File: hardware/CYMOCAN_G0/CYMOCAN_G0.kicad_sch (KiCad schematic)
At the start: 38 parts, among them J1 105450-0101, J2 CAN2 TX|RX, J3 Conn_01x02_Pin, J4 Conn_01x02_Pin, J5 CAN2, J6 DebugEdge_02x05, J7 CAN1 TX|RX, J8 CAN1, SW1 Reset, U1 AP2112K-3.3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

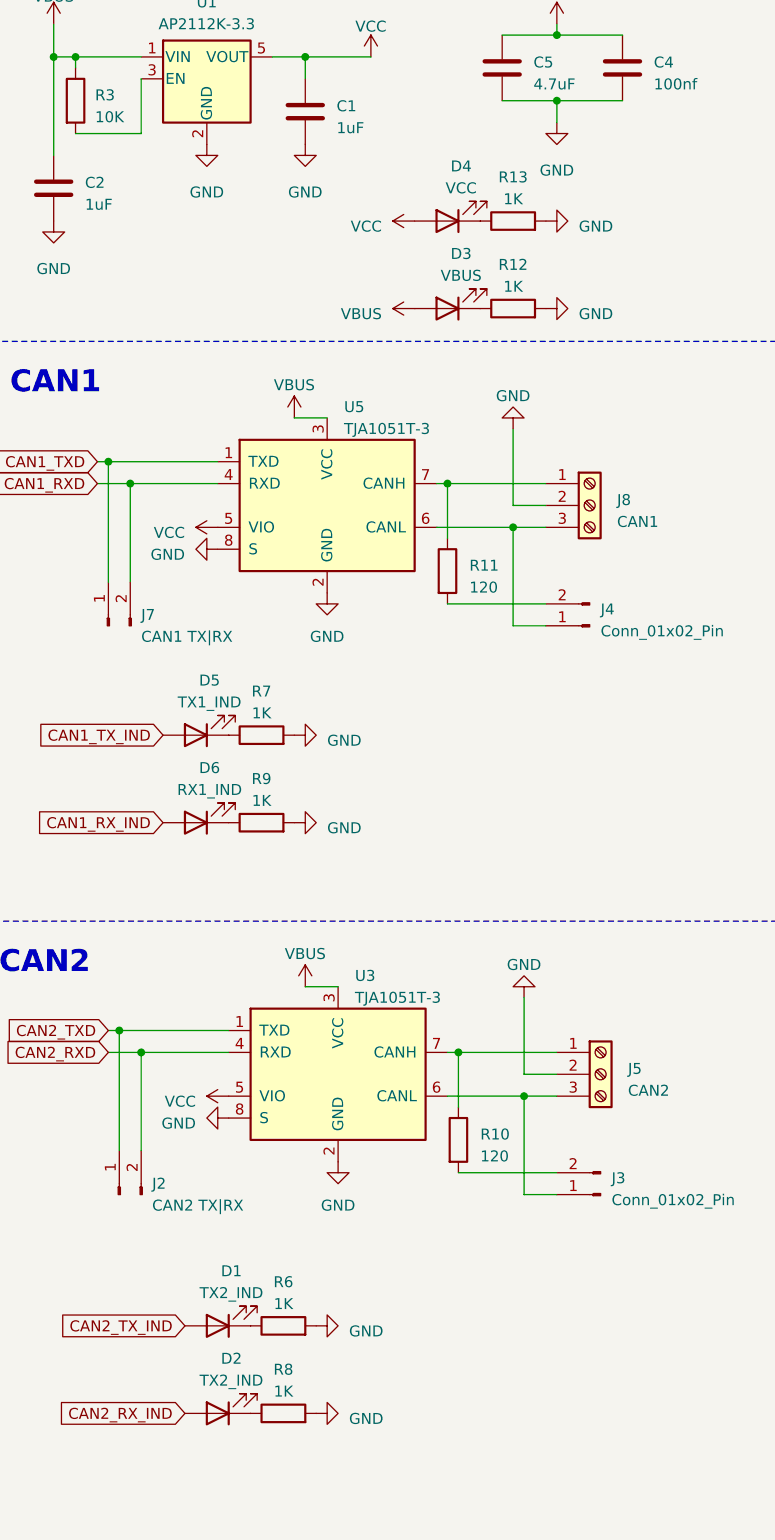
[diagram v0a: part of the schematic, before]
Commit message: Fix Led Resistor values
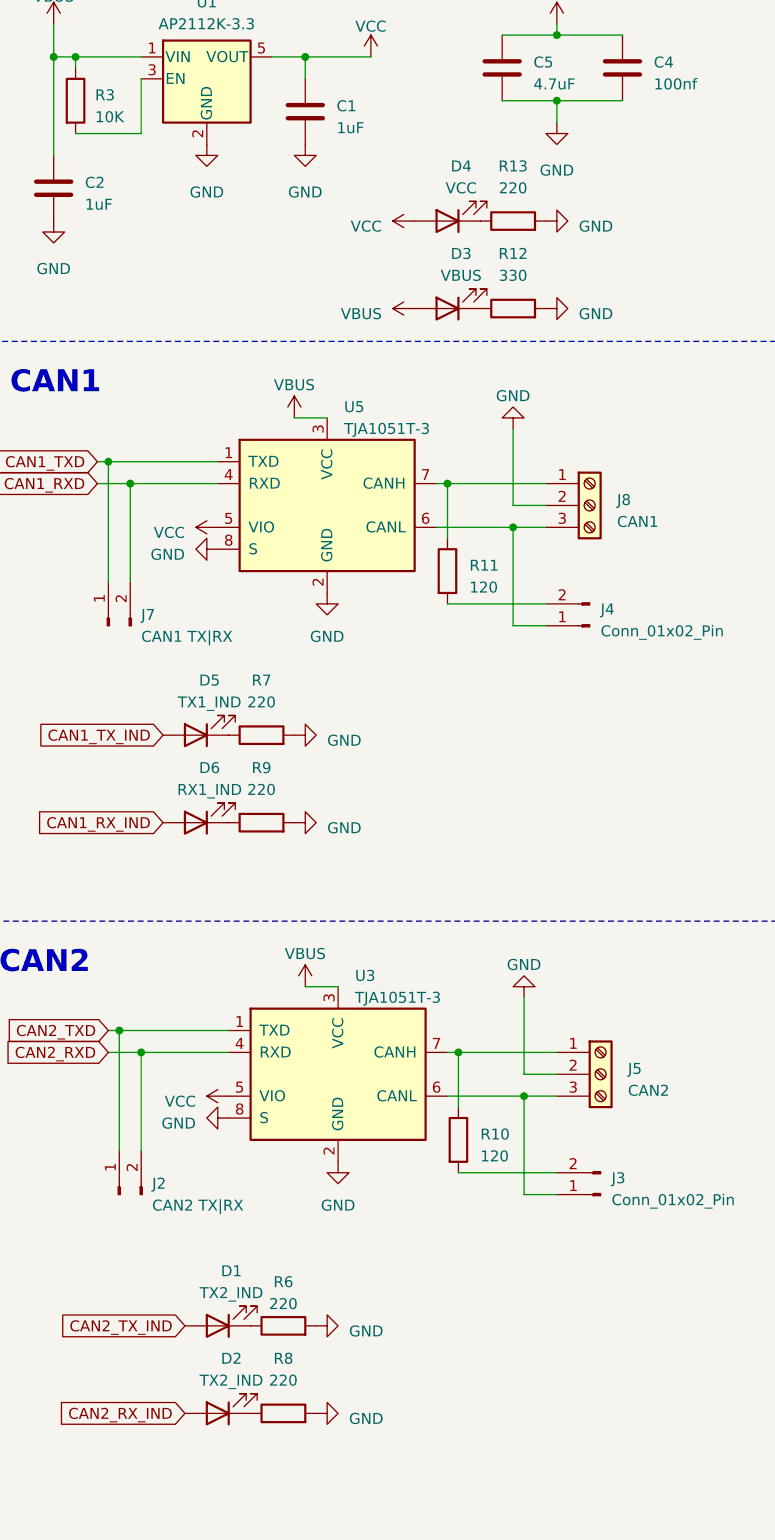
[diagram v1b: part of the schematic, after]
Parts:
- R12: value 1K -> 330
- R13, R6, R7, R8, R9: value 1K -> 220
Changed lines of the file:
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@@
   (symbol (lib_id "Device:R") (at 50.8 185.42 90) (unit 1)
     (in_bom yes) (on_board yes) (dnp no) (fields_autoplaced)
-    (property "Reference" "R8" (at 50.8 180.34 90)
-      (effects (font (size 1.27 1.27)))
-    )
-    (property "Value" "1K" (at 50.8 182.88 90)
+    (property "Reference" "R8" (at 50.8 179.07 90)
+      (effects (font (size 1.27 1.27)))
+    )
+    (property "Value" "220" (at 50.8 181.61 90)
       (effects (font (size 1.27 1.27)))
     )
@@
   (symbol (lib_id "Device:R") (at 77.47 46.99 90) (unit 1)
     (in_bom yes) (on_board yes) (dnp no) (fields_autoplaced)
-    (property "Reference" "R13" (at 77.47 41.91 90)
-      (effects (font (size 1.27 1.27)))
-    )
-    (property "Value" "1K" (at 77.47 44.45 90)
+    (property "Reference" "R13" (at 77.47 40.64 90)
+      (effects (font (size 1.27 1.27)))
+    )
+    (property "Value" "220" (at 77.47 43.18 90)
       (effects (font (size 1.27 1.27)))
     )
@@
   (symbol (lib_id "Device:R") (at 48.26 106.68 90) (unit 1)
     (in_bom yes) (on_board yes) (dnp no) (fields_autoplaced)
-    (property "Reference" "R7" (at 48.26 101.6 90)
-      (effects (font (size 1.27 1.27)))
-    )
-    (property "Value" "1K" (at 48.26 104.14 90)
+    (property "Reference" "R7" (at 48.26 100.33 90)
+      (effects (font (size 1.27 1.27)))
+    )
+    (property "Value" "220" (at 48.26 102.87 90)
       (effects (font (size 1.27 1.27)))
     )
@@
   (symbol (lib_id "Device:R") (at 48.26 116.84 90) (unit 1)
     (in_bom yes) (on_board yes) (dnp no) (fields_autoplaced)
-    (property "Reference" "R9" (at 48.26 111.76 90)
-      (effects (font (size 1.27 1.27)))
-    )
-    (property "Value" "1K" (at 48.26 114.3 90)
+    (property "Reference" "R9" (at 48.26 110.49 90)
+      (effects (font (size 1.27 1.27)))
+    )
+    (property "Value" "220" (at 48.26 113.03 90)
       (effects (font (size 1.27 1.27)))
     )
@@
   (symbol (lib_id "Device:R") (at 77.47 57.15 90) (unit 1)
     (in_bom yes) (on_board yes) (dnp no) (fields_autoplaced)
-    (property "Reference" "R12" (at 77.47 52.07 90)
-      (effects (font (size 1.27 1.27)))
-    )
-    (property "Value" "1K" (at 77.47 54.61 90)
+    (property "Reference" "R12" (at 77.47 50.8 90)
+      (effects (font (size 1.27 1.27)))
+    )
+    (property "Value" "330" (at 77.47 53.34 90)
       (effects (font (size 1.27 1.27)))
     )
@@
       (effects (font (size 1.27 1.27)))
     )
-    (property "Value" "1K" (at 50.8 172.72 90)
-      (effects (font (size 1.27 1.27)))
-    )
+    (property "Value" "220" (at 50.8 172.72 90)
+      (effects (font (size 1.27 1.27)))
+    )

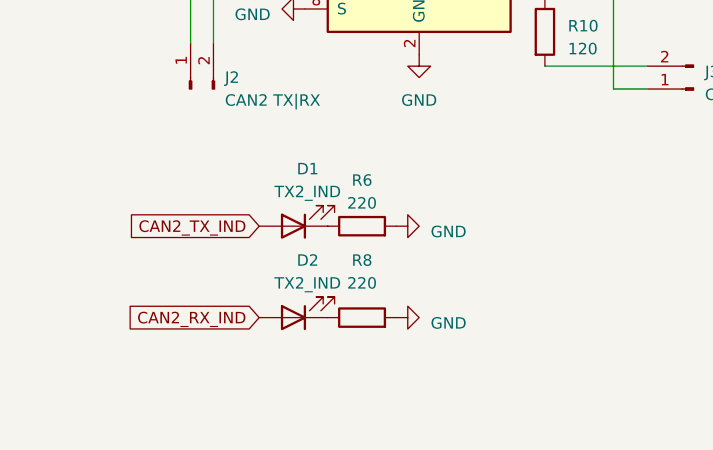
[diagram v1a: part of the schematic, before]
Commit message: Fix typo in D2 LED label
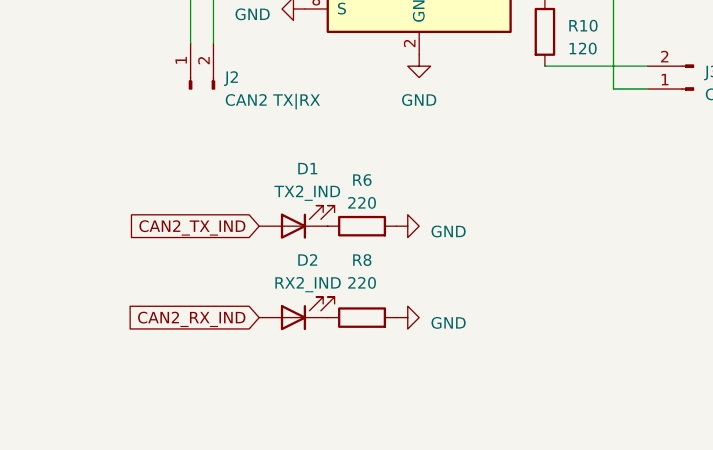
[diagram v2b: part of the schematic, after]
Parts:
- D2: value TX2_IND -> RX2_IND
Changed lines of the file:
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@@
   )
   (symbol (lib_id "Device:LED") (at 43.18 185.42 180) (unit 1)
-    (in_bom yes) (on_board yes) (dnp no) (fields_autoplaced)
+    (in_bom yes) (on_board yes) (dnp no)
     (property "Reference" "D2" (at 44.7675 179.07 0)
       (effects (font (size 1.27 1.27)))
     )
-    (property "Value" "TX2_IND" (at 44.7675 181.61 0)
+    (property "Value" "RX2_IND" (at 44.7675 181.61 0)
       (effects (font (size 1.27 1.27)))
     )
